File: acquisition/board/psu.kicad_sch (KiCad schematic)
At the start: 0 parts

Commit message: Continued initial design
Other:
- company: (none) -> A. Zonenberg
- title: (none) -> Digitizer board
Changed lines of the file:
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@@
 (kicad_sch (version 20211123) (generator eeschema)
   (paper "A4")
+  (title_block
+    (title "Digitizer board")
+    (date "2022-06-22")
+    (rev "0.1")
+    (company "A. Zonenberg")
+  )
+  (hierarchical_label "A1V8" (shape output) (at 76.2 113.03 0)
+    (effects (font (size 1.27 1.27)) (justify left))
+  )
+  (hierarchical_label "GND" (shape output) (at 76.2 124.46 0)
+    (effects (font (size 1.27 1.27)) (justify left))
+  )
+  (hierarchical_label "3V3" (shape output) (at 73.66 102.87 0)
+    (effects (font (size 1.27 1.27)) (justify left))
+  )
+  (hierarchical_label "1V0" (shape output) (at 76.2 119.38 0)
+    (effects (font (size 1.27 1.27)) (justify left))
+  )
+  (hierarchical_label "2V5" (shape output) (at 77.47 132.08 0)
+    (effects (font (size 1.27 1.27)) (justify left))
+  )
+  (hierarchical_label "D1V8" (shape output) (at 76.2 115.57 0)
+    (effects (font (size 1.27 1.27)) (justify left))
+  )
+  (hierarchical_label "VREF" (shape output) (at 74.93 87.63 0)
+    (effects (font (size 1.27 1.27)) (justify left))
+  )
 )

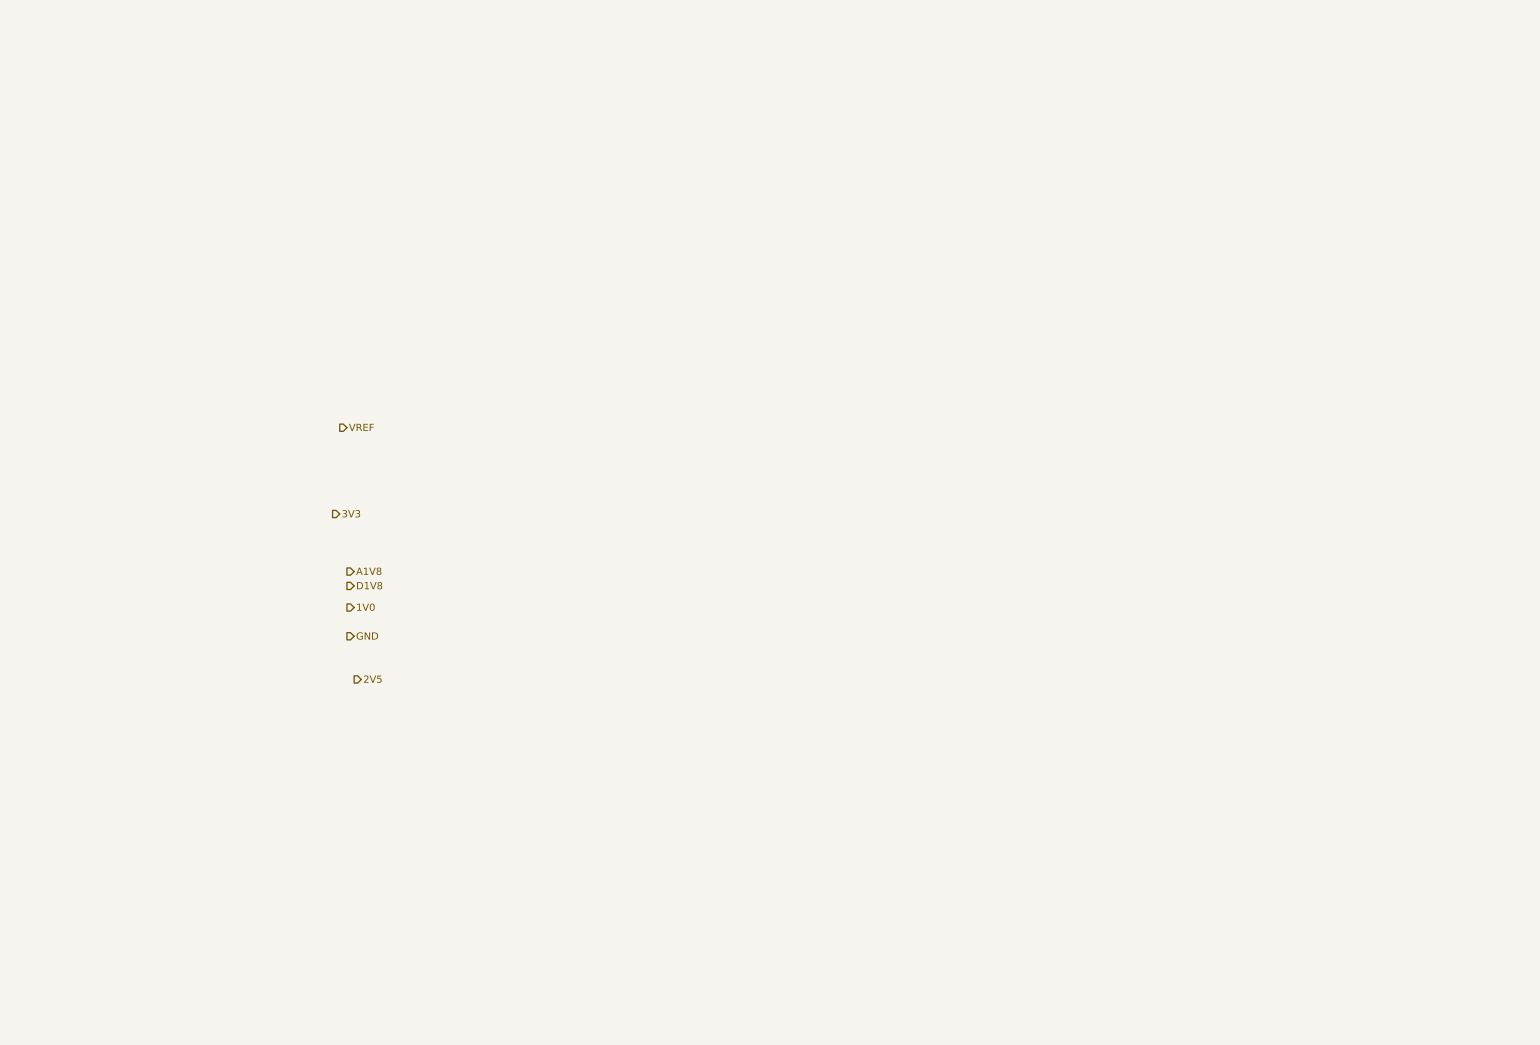
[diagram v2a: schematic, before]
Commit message: Lots of progress on power supply design, added a bunch of test points, etc
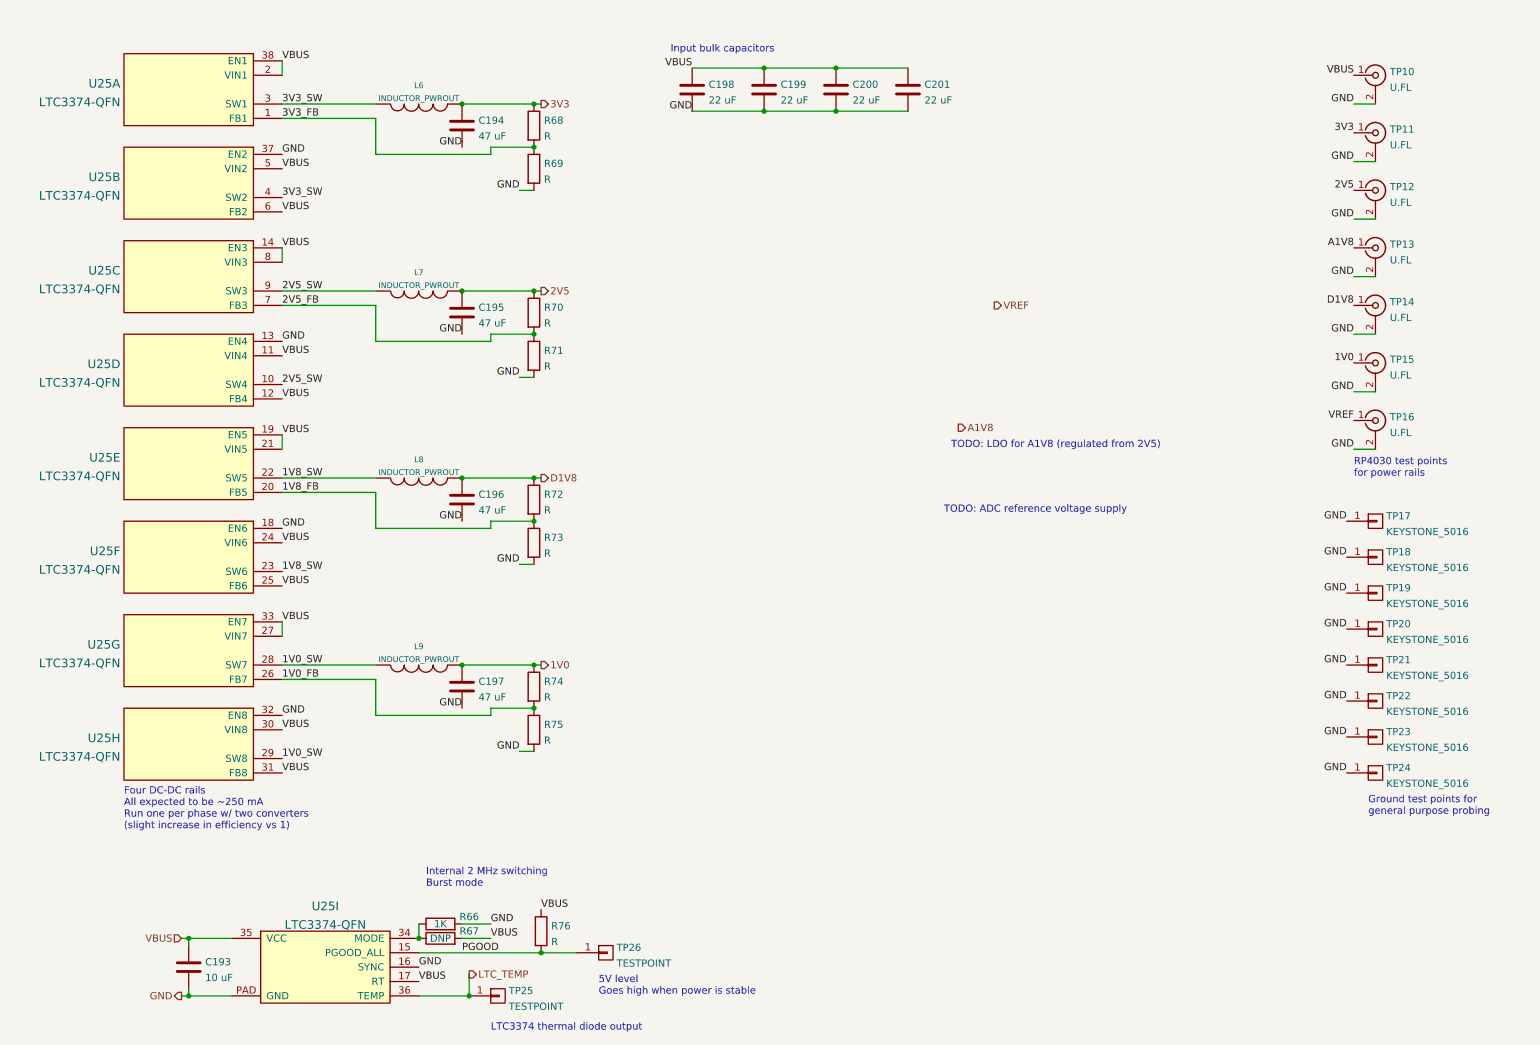
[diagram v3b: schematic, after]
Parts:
- added C193: 10 uF, symbol device:C
- added C194, C195, C196, C197: 47 uF, symbol device:C
- added C198, C199, C200, C201: 22 uF, symbol device:C
- added L6, L7, L8, L9: INDUCTOR_PWROUT, symbol passive-azonenberg:INDUCTOR_PWROUT
- added R66: 1K, symbol device:R
- added R67: DNP, symbol device:R
- added R68, R69, R70, R71, R72, R73, R74, R75, R76: R, symbol device:R
- added TP10, TP11, TP12, TP13, TP14, TP15, TP16: U.FL, symbol conn:CONN_COAXIAL
- added TP17, TP18, TP19, TP20, TP21, TP22, TP23, TP24: KEYSTONE_5016, symbol conn:CONN_01X01
- added TP25, TP26: TESTPOINT, symbol conn:CONN_01X01
- added U25: LTC3374-QFN, symbol power-azonenberg:LTC3374-QFN
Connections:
- net 1V0: now also C197.1, L9.2, R74.1, TP15.1 (In)
- net 2V5: now also C195.1, L7.2, R70.1, TP12.1 (In)
- net 3V3: now also C194.1, L6.2, R68.1, TP11.1 (In)
- net A1V8: now also TP13.1 (In)
- net D1V8: now also C196.1, L8.2, R72.1, TP14.1 (In)
- net GND: now also C193.2, C194.2, C195.2, C196.2, C197.2, C198.2, C199.2, C200.2, C201.2, R66.2, R69.2, R71.2, R73.2, R75.2, TP10.2 (Ext), TP11.2 (Ext), TP12.2 (Ext), TP13.2 (Ext), TP14.2 (Ext), TP15.2 (Ext), TP16.2 (Ext), TP17.1 (P1), TP18.1 (P1), TP19.1 (P1), TP20.1 (P1), TP21.1 (P1), TP22.1 (P1), TP23.1 (P1), TP24.1 (P1), U25.13 (EN4), U25.16 (SYNC), U25.18 (EN6), U25.32 (EN8), U25.37 (EN2), U25.PAD (GND)
- net VREF: now also TP16.1 (In)
- new net: R66.1, R67.1, U25.34 (MODE)
- new net 1V0_FB: R74.2, R75.1, U25.26 (FB7)
- new net 1V0_SW: L9.1, U25.28 (SW7), U25.29 (SW8)
- new net 1V8_FB: R72.2, R73.1, U25.20 (FB5)
- new net 1V8_SW: L8.1, U25.22 (SW5), U25.23 (SW6)
- new net 2V5_FB: R70.2, R71.1, U25.7 (FB3)
- new net 2V5_SW: L7.1, U25.10 (SW4), U25.9 (SW3)
- new net 3V3_FB: R68.2, R69.1, U25.1 (FB1)
- new net 3V3_SW: L6.1, U25.3 (SW1), U25.4 (SW2)
- new net LTC_TEMP: TP25.1 (P1), U25.36 (TEMP)
- new net PGOOD: R76.2, TP26.1 (P1), U25.15 (PGOOD_ALL)
- new net VBUS: C193.1, C198.1, C199.1, C200.1, C201.1, R67.2, R76.1, TP10.1 (In), U25.11 (VIN4), U25.12 (FB4), U25.14 (EN3), U25.17 (RT), U25.19 (EN5), U25.2 (VIN1), U25.21 (VIN5), U25.24 (VIN6), U25.25 (FB6), U25.27 (VIN7), U25.30 (VIN8), U25.31 (FB8), U25.33 (EN7), U25.35 (VCC), U25.38 (EN1), U25.5 (VIN2), U25.6 (FB2), U25.8 (VIN3)
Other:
- note added: "5V level Goes high when power is stable"
- note added: "Four DC-DC rails All expected to be ~250 mA Run one per phase w/ two converters (slight increase in efficiency vs 1)"
- note added: "Ground test points for general purpose probing"
- note added: "Input bulk capacitors"
- note added: "Internal 2 MHz switching Burst mode"
- note added: "LTC3374 thermal diode output"
- note added: "RP4030 test points for power rails"
- note added: "TODO: ADC reference voltage supply"
- note added: "TODO: LDO for A1V8 (regulated from 2V5)"

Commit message: More power supply work, added PLL loop filter, soft start, began assigning footprints
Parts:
- added C210, C211, C212, C213, C216, C217: DNP, azonenberg_pcb:EIA_0402_CAP_NOSILK, symbol device:C
- added C214, C215, C218, C219, C221, C222: 4.7 uF, azonenberg_pcb:EIA_0603_CAP_NOSILK, symbol device:C
- added R77: 470, azonenberg_pcb:EIA_0402_RES_NOSILK, symbol device:R
- added R78, R79: 18K, symbol device:R
- added TP27: U.FL, azonenberg_pcb:CONN_U.FL_TE_1909763-1, symbol conn:CONN_COAXIAL
- added U26, U27: LT3042, symbol power-azonenberg:LT3042
- added U28: ADR510, symbol analog-azonenberg:ADR510
- added U30: LDO1117-12, symbol passive-azonenberg:LDO1117-XX
- L6, L7, L8, L9: value INDUCTOR_PWROUT -> NRS5030T2R2NMGJ; footprint (none) -> azonenberg_pcb:INDUCTOR_YUDEN_NRS5030
- R66, R67: footprint (none) -> azonenberg_pcb:EIA_0402_RES_NOSILK
- R68, R70, R75: value R -> 1.02M
- R69: value R -> 324K
- R71: value R -> 475K
- R72: value R -> 806K
- R73: value R -> 649K
- R74: value R -> 255K
- R76: value R -> 10K; footprint (none) -> azonenberg_pcb:EIA_0402_RES_NOSILK
- TP10, TP11, TP12, TP13, TP14, TP15, TP16: footprint (none) -> azonenberg_pcb:CONN_U.FL_TE_1909763-1
- TP17, TP18, TP19, TP20, TP21, TP22, TP23, TP24: footprint (none) -> azonenberg_pcb:TESTPOINT_SMT_KEYSTONE_5016
- TP25, TP26: footprint (none) -> azonenberg_pcb:TESTPOINT_SMT_0.5MM
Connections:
- net 1V0: now also L9.1, C213.1; no longer L9.2
- net 1V0_FB: now also C213.2
- net 1V0_SW: now also L9.2; no longer L9.1
- net 1V8_FB: now also C212.2
- net 1V8_SW: now also L8.2; no longer L8.1
- net 2V5: now also L7.1, C211.1, C214.1, C215.1, C221.1, U26.1 (IN), U26.2 (IN), U26.3 (EN/UV), U26.6 (PGFB), U27.1 (IN), U27.2 (IN), U27.3 (EN/UV), U27.6 (PGFB), U30.3 (Vin); no longer L7.2
- net 2V5_FB: now also C211.2
- net 2V5_SW: now also L7.2; no longer L7.1
- net 3V3: now also L6.1, C210.1; no longer L6.2
- net 3V3_FB: now also C210.2
- net 3V3_SW: now also L6.2; no longer L6.1
- net D1V8: now also L8.1, C212.1; no longer L8.2
- net GND: now also C214.2, C215.2, C216.2, C217.2, C218.2, C219.2, C221.2, C222.2, R78.2, R79.2, TP27.2 (Ext), U26.5 (ILIM), U26.8 (GND), U26.PAD (GND), U27.5 (ILIM), U27.8 (GND), U27.PAD (GND), U28.2 (V-), U30.1 (Gnd)
- net VREF: now also R77.1, U28.1 (V+)
- net A1V8 renamed A1V8_1
- net A1V8_1: now also C218.1, R77.2, U26.10 (OUT), U26.9 (OUTS)
- new net 1V2: C222.1, U30.2 (Vout)
- new net A1V8_1_SET: C216.1, R78.1, U26.7 (SET)
- new net A1V8_2: C219.1, TP27.1 (In), U27.10 (OUT), U27.9 (OUTS)
- new net A1V8_2_SET: C217.1, R79.1, U27.7 (SET)
- no-connect marks 0 -> 3
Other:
- note added: "1.0V ADC reference voltage supply Expected load ~533 uA Rbias = (1.8V - 1.0V) / (533 uA + Iq) Target Iq = 1 mA (cannot exceed 10 mA) Rbias = 800 mV / 1.533 mA = 521 ohms With Rbias = 470 ohms, Iq = 1.169 mA"
- note added: "1.8V analog supply rails LT3042 is rated for 200 mA, but ADCs need 53 mA Split load across two rails, 106 mA each 2.5V in -> 1.8V out is 700 mV drop 700 mV * 106 mA = 75 mW 34.4 C/W so expect only 2.58C temp rise Vset = 100 uA * Rset Rset = Vset / 100 uA = 18K"
- note added: "Four DC-DC rails All expected to be ~250 mA Parallel two converters per rail (slight increase in efficiency vs 1), one phase per rail"
- note added: "ice40 core power rail Expecting <25 mA worst case, probably single digit mA"
- note removed: "Four DC-DC rails All expected to be ~250 mA Run one per phase w/ two converters (slight increase in efficiency vs 1)"
- note removed: "TODO: ADC reference voltage supply"
- note removed: "TODO: LDO for A1V8 (regulated from 2V5)"
- moved on the sheet: C194, C195, C196, C197, C198, C199, C200, C201, L6, L7, L8, L9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

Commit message: Completed schematic after design review, ready for layout
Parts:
- C193, C194, C195, C196, C197: footprint (none) -> azonenberg_pcb:EIA_1206_CAP_NOSILK
- C198, C199, C200, C201: footprint (none) -> azonenberg_pcb:EIA_1210_CAP_NOSILK
- R68, R69, R70, R71, R72, R73, R74, R75, R78, R79: footprint (none) -> azonenberg_pcb:EIA_0402_RES_NOSILK
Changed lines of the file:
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@@
   (title_block
     (title "Digitizer board")
-    (date "2022-07-08")
+    (date "2022-07-17")
     (rev "0.1")
     (company "A. Zonenberg")
@@
       (effects (font (size 1.27 1.27)) (justify left))
     )
-    (property "Footprint" "" (id 2) (at 96.2152 130.81 0)
+    (property "Footprint" "azonenberg_pcb:EIA_1206_CAP_NOSILK" (id 2) (at 96.2152 130.81 0)
       (effects (font (size 1.27 1.27)) hide)
     )
@@
       (effects (font (size 1.27 1.27)) (justify left))
     )
-    (property "Footprint" "" (id 2) (at 49.2252 186.69 0)
+    (property "Footprint" "azonenberg_pcb:EIA_1206_CAP_NOSILK" (id 2) (at 49.2252 186.69 0)
       (effects (font (size 1.27 1.27)) hide)
     )
@@
       (effects (font (size 1.27 1.27)) (justify left))
     )
-    (property "Footprint" "" (id 2) (at 106.172 127 90)
+    (property "Footprint" "azonenberg_pcb:EIA_0402_RES_NOSILK" (id 2) (at 106.172 127 90)
       (effects (font (size 1.27 1.27)) hide)
     )
@@
       (effects (font (size 1.27 1.27)) (justify left))
     )
-    (property "Footprint" "" (id 2) (at 174.752 142.24 90)
+    (property "Footprint" "azonenberg_pcb:EIA_0402_RES_NOSILK" (id 2) (at 174.752 142.24 90)
       (effects (font (size 1.27 1.27)) hide)
     )
@@
       (effects (font (size 1.27 1.27)) (justify left))
     )
-    (property "Footprint" "" (id 2) (at 106.172 35.56 90)
+    (property "Footprint" "azonenberg_pcb:EIA_0402_RES_NOSILK" (id 2) (at 106.172 35.56 90)
       (effects (font (size 1.27 1.27)) hide)
     )
@@
       (effects (font (size 1.27 1.27)) (justify left))
     )
-    (property "Footprint" "" (id 2) (at 96.2152 31.75 0)
+    (property "Footprint" "azonenberg_pcb:EIA_1206_CAP_NOSILK" (id 2) (at 96.2152 31.75 0)
       (effects (font (size 1.27 1.27)) hide)
     )
@@
       (effects (font (size 1.27 1.27)) (justify left))
     )
-    (property "Footprint" "" (id 2) (at 96.2152 64.77 0)
+    (property "Footprint" "azonenberg_pcb:EIA_1206_CAP_NOSILK" (id 2) (at 96.2152 64.77 0)
       (effects (font (size 1.27 1.27)) hide)
     )
@@
       (effects (font (size 1.27 1.27)) (justify left))
     )
-    (property "Footprint" "" (id 2) (at 50.4952 166.37 0)
+    (property "Footprint" "azonenberg_pcb:EIA_1210_CAP_NOSILK" (id 2) (at 50.4952 166.37 0)
       (effects (font (size 1.27 1.27)) hide)
     )
@@
       (effects (font (size 1.27 1.27)) (justify left))
     )
-    (property "Footprint" "" (id 2) (at 174.752 115.57 90)
+    (property "Footprint" "azonenberg_pcb:EIA_0402_RES_NOSILK" (id 2) (at 174.752 115.57 90)
       (effects (font (size 1.27 1.27)) hide)
     )
@@
       (effects (font (size 1.27 1.27)) (justify left))
     )
-    (property "Footprint" "" (id 2) (at 106.172 68.58 90)
+    (property "Footprint" "azonenberg_pcb:EIA_0402_RES_NOSILK" (id 2) (at 106.172 68.58 90)
       (effects (font (size 1.27 1.27)) hide)
     )
@@
       (effects (font (size 1.27 1.27)) (justify left))
     )
-    (property "Footprint" "" (id 2) (at 75.8952 166.37 0)
+    (property "Footprint" "azonenberg_pcb:EIA_1210_CAP_NOSILK" (id 2) (at 75.8952 166.37 0)
       (effects (font (size 1.27 1.27)) hide)
     )
@@
       (effects (font (size 1.27 1.27)) (justify left))
     )
-    (property "Footprint" "" (id 2) (at 106.172 27.94 90)
+    (property "Footprint" "azonenberg_pcb:EIA_0402_RES_NOSILK" (id 2) (at 106.172 27.94 90)
       (effects (font (size 1.27 1.27)) hide)
     )
@@
       (effects (font (size 1.27 1.27)) (justify left))
     )
-    (property "Footprint" "" (id 2) (at 63.1952 166.37 0)
+    (property "Footprint" "azonenberg_pcb:EIA_1210_CAP_NOSILK" (id 2) (at 63.1952 166.37 0)
       (effects (font (size 1.27 1.27)) hide)
     )
@@
       (effects (font (size 1.27 1.27)) (justify left))
     )
-    (property "Footprint" "" (id 2) (at 37.7952 166.37 0)
+    (property "Footprint" "azonenberg_pcb:EIA_1210_CAP_NOSILK" (id 2) (at 37.7952 166.37 0)
       (effects (font (size 1.27 1.27)) hide)
     )
@@
       (effects (font (size 1.27 1.27)) (justify left))
     )
-    (property "Footprint" "" (id 2) (at 106.172 134.62 90)
+    (property "Footprint" "azonenberg_pcb:EIA_0402_RES_NOSILK" (id 2) (at 106.172 134.62 90)
       (effects (font (size 1.27 1.27)) hide)
     )
@@
       (effects (font (size 1.27 1.27)) (justify left))
     )
-    (property "Footprint" "" (id 2) (at 106.172 101.6 90)
+    (property "Footprint" "azonenberg_pcb:EIA_0402_RES_NOSILK" (id 2) (at 106.172 101.6 90)
       (effects (font (size 1.27 1.27)) hide)
     )
@@
       (effects (font (size 1.27 1.27)) (justify left))
     )
-    (property "Footprint" "" (id 2) (at 106.172 93.98 90)
+    (property "Footprint" "azonenberg_pcb:EIA_0402_RES_NOSILK" (id 2) (at 106.172 93.98 90)
       (effects (font (size 1.27 1.27)) hide)
     )
@@
       (effects (font (size 1.27 1.27)) (justify left))
     )
-    (property "Footprint" "" (id 2) (at 106.172 60.96 90)
+    (property "Footprint" "azonenberg_pcb:EIA_0402_RES_NOSILK" (id 2) (at 106.172 60.96 90)
       (effects (font (size 1.27 1.27)) hide)
     )
@@
       (effects (font (size 1.27 1.27)) (justify left))
     )
-    (property "Footprint" "" (id 2) (at 96.2152 97.79 0)
-      (effects (font (size 1.27 1.27)) hide)
-    )
+    (property "Footprint" "azonenberg_pcb:EIA_1206_CAP_NOSILK" (id 2) (at 96.2152 97.79 0)
+      (effects (font (size 1.27 1.27)) hide)
+    )
